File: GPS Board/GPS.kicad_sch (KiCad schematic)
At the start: 50 parts, among them J101 USB_B_Micro, J102 Conn_01x05, J103 Conn_01x08_Female, J104 Conn_01x06_Female, U101 AP7361C-10E, U102 AZ1117-3.3, U103 AZ1117-3.3, U104 SMA_CONN, U105 M10578-A2, U106 MCP2562-H-SN, U107 STM32F103C8T6, Y101 8MHz

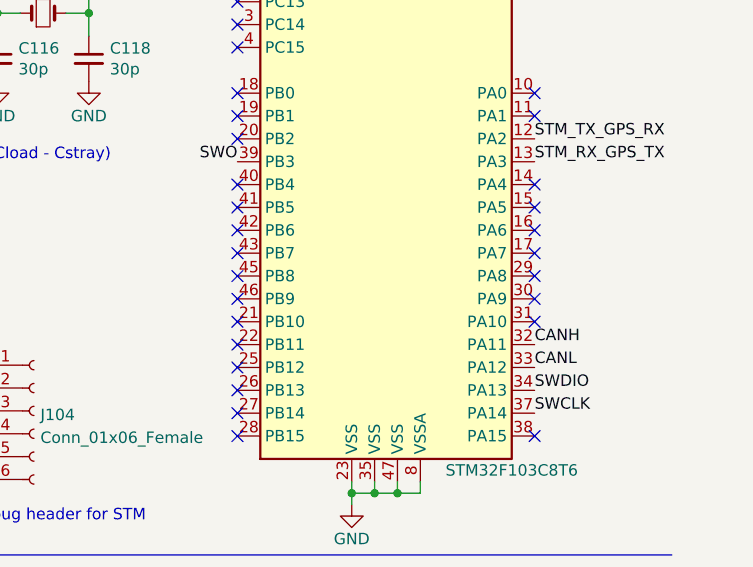
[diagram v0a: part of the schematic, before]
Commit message: Updated GPS Board Schematic, still need to remake board
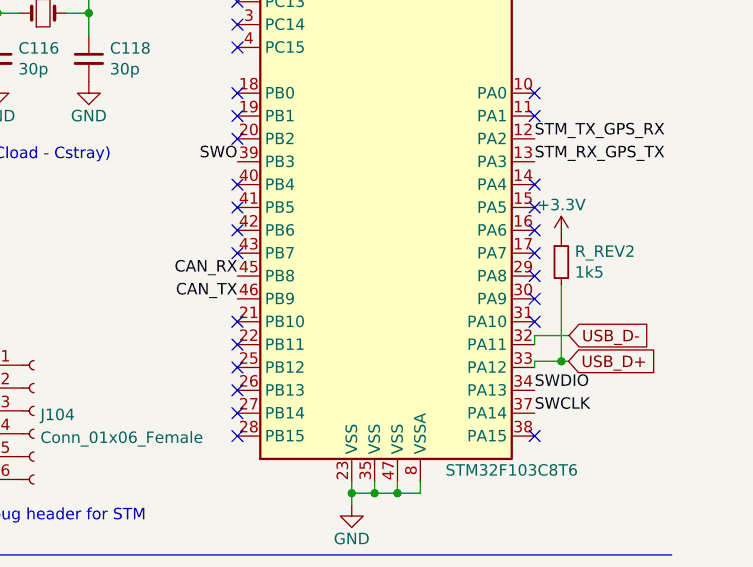
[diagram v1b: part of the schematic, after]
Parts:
- added R_REV2: 1k5, Resistor_SMD:R_0805_2012Metric, symbol Device:R_Small
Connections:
- net +3.3V: now also R_REV2.1
- net CANH: no longer U107.32 (PA11)
- net CANL: no longer U107.33 (PA12)
- net CAN_RX: now also U107.45 (PB8)
- net CAN_TX: now also U107.46 (PB9)
- net USB_D+: now also U107.33 (PA12), R_REV2.2
- net USB_D-: now also U107.32 (PA11)
- no-connect marks 34 -> 32
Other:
- company: Atharva Kulkarni -> Atharva Kulkarni and Dylan Haussecker
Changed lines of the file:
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@@
     (date "2023-02-04")
     (rev "A")
-    (company "Atharva Kulkarni")
+    (company "Atharva Kulkarni and Dylan Haussecker")
     (comment 1 "USST Rocket ")
   )
@@
   )
   (junction (at 105.41 163.83) (diameter 0) (color 0 0 0 0)
+  )
+  (junction (at 273.4818 119.4565) (diameter 0) (color 0 0 0 0)
   )
   (junction (at 88.9 95.25) (diameter 0) (color 0 0 0 0)
@@
   (no_connect (at 270.51 92.202))
   (no_connect (at 237.49 104.902))
-  (no_connect (at 237.49 109.982))
   (no_connect (at 237.49 89.662))
-  (no_connect (at 237.49 112.522))
   (no_connect (at 270.51 107.442))
   (no_connect (at 109.22 146.05))
@@
     (stroke (width 0) (type default) (color 0 0 0 0))
   )
+  (wire (pts (xy 270.51 119.4565) (xy 273.4818 119.4565))
+    (stroke (width 0) (type default) (color 0 0 0 0))
+  )
   (wire (pts (xy 140.97 34.29) (xy 140.97 48.26))
     (stroke (width 0) (type default) (color 0 0 0 0))
@@
     (stroke (width 0) (type default) (color 0 0 0 0))
   )
+  (wire (pts (xy 270.51 119.4565) (xy 270.51 120.142))
+    (stroke (width 0) (type default) (color 0 0 0 0))
+  )
   (polyline (pts (xy 91.44 87.63) (xy 91.44 81.28))
     (stroke (width 0) (type default) (color 0 0 0 0))
@@
     (stroke (width 0) (type default) (color 0 0 0 0))
   )
+  (wire (pts (xy 273.4818 110.9728) (xy 273.4818 119.4565))
+    (stroke (width 0) (type default) (color 0 0 0 0))
+  )
   (wire (pts (xy 120.65 167.64) (xy 120.65 171.704))
     (stroke (width 0) (type default) (color 0 0 0 0))
@@
     (stroke (width 0) (type default) (color 0 0 0 0))
   )
+  (wire (pts (xy 274.3367 116.598) (xy 270.51 116.598))
+    (stroke (width 0) (type default) (color 0 0 0 0))
+  )
   (wire (pts (xy 240.284 43.18) (xy 240.284 41.91))
     (stroke (width 0) (type default) (color 0 0 0 0))
@@
     (stroke (width 0) (type default) (color 0 0 0 0))
   )
+  (wire (pts (xy 273.4818 119.4565) (xy 274.279 119.4565))
+    (stroke (width 0) (type default) (color 0 0 0 0))
+  )
   (polyline (pts (xy 127 81.28) (xy 127 114.046))
     (stroke (width 0) (type default) (color 0 0 0 0))
@@
   )
   (wire (pts (xy 270.002 27.432) (xy 270.002 26.162))
+    (stroke (width 0) (type default) (color 0 0 0 0))
+  )
+  (wire (pts (xy 270.51 116.598) (xy 270.51 117.602))
     (stroke (width 0) (type default) (color 0 0 0 0))
   )
@@
     (effects (font (size 1.27 1.27)) (justify left bottom))
   )
+  (label "CAN_RX" (at 237.49 109.982 180)
+    (effects (font (size 1.27 1.27)) (justify right bottom))
+  )
   (label "V_in" (at 52.07 62.23 0)
     (effects (font (size 1.27 1.27)) (justify left bottom))
@@
     (effects (font (size 1.27 1.27)) (justify left bottom))
   )
+  (label "CAN_TX" (at 237.49 112.522 180)
+    (effects (font (size 1.27 1.27)) (justify right bottom))
+  )
   (label "RF_IN" (at 102.87 110.49 180)
     (effects (font (size 1.27 1.27)) (justify right bottom))
@@
     (effects (font (size 1.27 1.27)) (justify left bottom))
   )
-  (label "CANL" (at 270.51 120.142 0)
-    (effects (font (size 1.27 1.27)) (justify left bottom))
-  )
   (label "V_in" (at 25.4 110.49 0)
     (effects (font (size 1.27 1.27)) (justify left bottom))
@@
     (effects (font (size 1.27 1.27)) (justify left bottom))
   )
-  (label "CANH" (at 270.51 117.602 0)
-    (effects (font (size 1.27 1.27)) (justify left bottom))
+  (global_label "USB_D-" (shape input) (at 274.3367 116.598 0) (fields_autoplaced)
+    (effects (font (size 1.27 1.27)) (justify left))
+    (property "Intersheet References" "${INTERSHEET_REFS}" (id 0) (at 220.9967 54.368 0)
+      (effects (font (size 1.27 1.27)) hide)
+    )
+  )
+  (global_label "USB_D+" (shape input) (at 274.279 119.4565 0) (fields_autoplaced)
+    (effects (font (size 1.27 1.27)) (justify left))
+    (property "Intersheet References" "${INTERSHEET_REFS}" (id 0) (at 220.939 59.7665 0)
+      (effects (font (size 1.27 1.27)) hide)
+    )
   )
   (global_label "USB_D-" (shape input) (at 27.94 167.64 0) (fields_autoplaced)
@@
       (effects (font (size 1.27 1.27)) hide)
     )
+  )
+  (symbol (lib_id "Device:R_Small") (at 273.4818 108.4328 0) (unit 1)
+    (in_bom yes) (on_board yes)
+    (property "Reference" "R_REV2" (id 0) (at 274.9804 107.2644 0)
+      (effects (font (size 1.27 1.27)) (justify left))
+    )
+    (property "Value" "1k5" (id 1) (at 274.9804 109.5758 0)
+      (effects (font (size 1.27 1.27)) (justify left))
+    )
+    (property "Footprint" "Resistor_SMD:R_0805_2012Metric" (id 2) (at 273.4818 108.4328 0)
+      (effects (font (size 1.27 1.27)) hide)
+    )
+    (property "Datasheet" "~" (id 3) (at 273.4818 108.4328 0)
+      (effects (font (size 1.27 1.27)) hide)
+    )
+    (property "LCSC Part #" "C22843" (id 4) (at 273.4818 108.4328 0)
+      (effects (font (size 1.27 1.27)) hide)
+    )
+    (pin "1")
+    (pin "2")
   )
   (symbol (lib_id "Device:LED_Small") (at 86.36 161.29 180) (unit 1)
@@
     )
     (property "Datasheet" "" (id 3) (at 45.72 118.11 0)
+      (effects (font (size 1.27 1.27)) hide)
+    )
+    (pin "1")
+  )
+  (symbol (lib_id "power:+3.3V") (at 273.4818 105.8928 0) (unit 1)
+    (in_bom yes) (on_board yes)
+    (property "Reference" "#PWR0150" (id 0) (at 273.4818 109.7028 0)
+      (effects (font (size 1.27 1.27)) hide)
+    )
+    (property "Value" "+3.3V" (id 1) (at 273.4818 102.0828 0))
+    (property "Footprint" "" (id 2) (at 273.4818 105.8928 0)
+      (effects (font (size 1.27 1.27)) hide)
+    )
+    (property "Datasheet" "" (id 3) (at 273.4818 105.8928 0)
       (effects (font (size 1.27 1.27)) hide)
     )
@@
       (reference "#PWR0149") (unit 1) (value "+3.3VA") (footprint "")
     )
+    (path "/5da13884-d0f5-4b34-aa0f-b6d2a86aed3f"
+      (reference "#PWR0150") (unit 1) (value "+3.3V") (footprint "")
+    )
     (path "/777bbcd9-c249-4587-88c2-5d4c41a194e6"
       (reference "C101") (unit 1) (value "4.7uF") (footprint "Capacitor_SMD:C_0805_2012Metric")
@@
       (reference "R104") (unit 1) (value "10k") (footprint "Resistor_SMD:R_0805_2012Metric_Pad1.20x1.40mm_HandSolder")
     )
+    (path "/1a5df665-d8d3-4911-b73d-91855719fe26"
+      (reference "R_REV2") (unit 1) (value "1k5") (footprint "Resistor_SMD:R_0805_2012Metric")
+    )
     (path "/0bc9a7df-41ad-4dff-9452-d9163128e5f3"
